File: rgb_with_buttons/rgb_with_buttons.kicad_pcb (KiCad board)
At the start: 2 copper layers, 17 parts, among them J4 Barrel_Jack_Switch, SW1 SW_MEC_5E, SW2 SW_MEC_5E, SW3 SW_MEC_5E, U1 ATmega328P-P

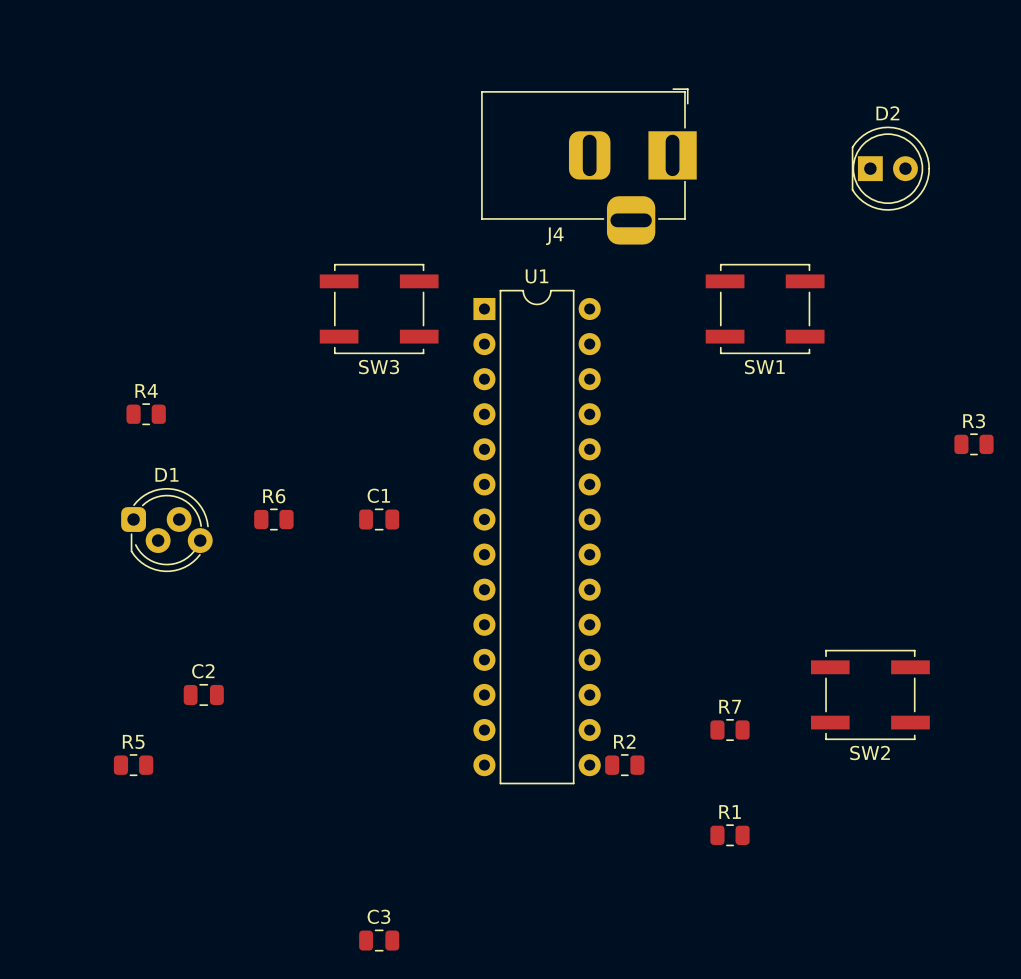
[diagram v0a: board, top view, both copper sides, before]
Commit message: all pcb is ready, not quite beautiful but functioning
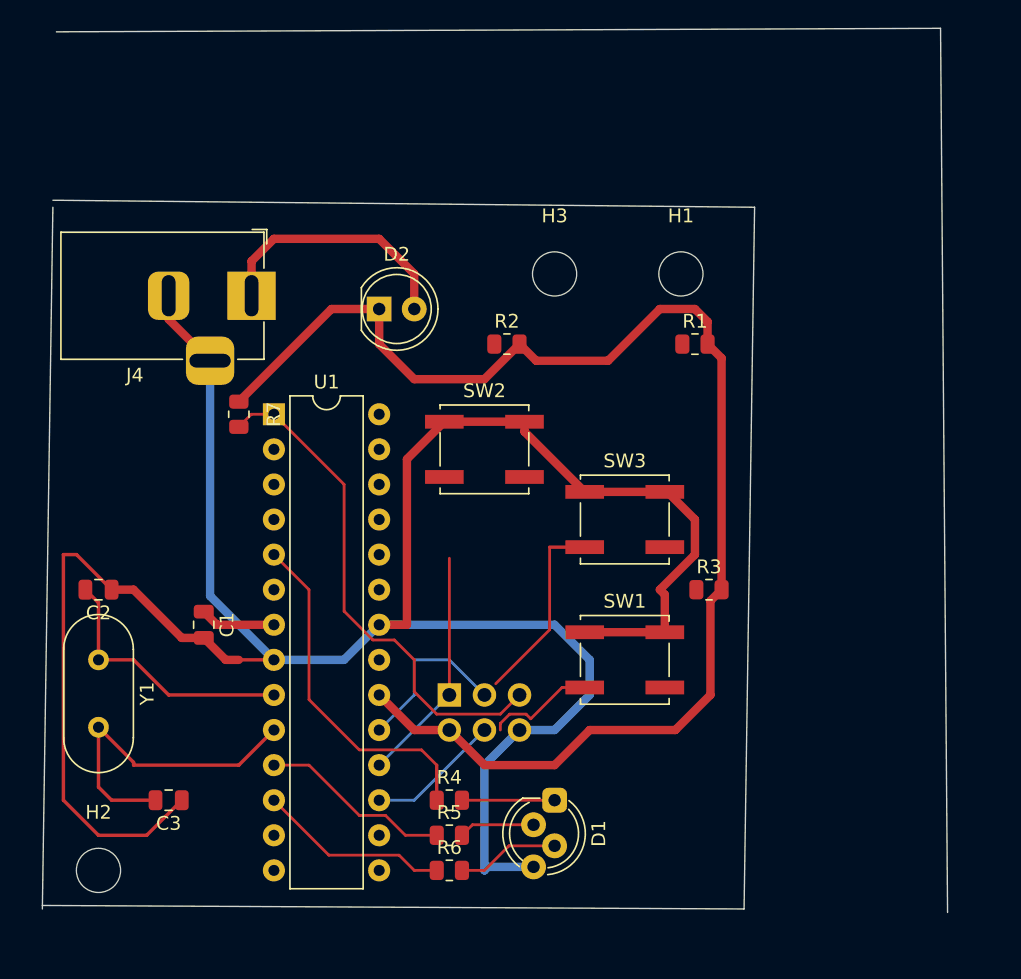
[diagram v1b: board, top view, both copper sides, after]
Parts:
- added H1: MountingHole, MountingHole:MountingHole_3.2mm_M3, F.Cu at (131.1, 81.3)
- added H2: MountingHole, MountingHole:MountingHole_3.2mm_M3, F.Cu at (88.9, 124.5)
- added H3: MountingHole, MountingHole:MountingHole_3.2mm_M3, F.Cu at (121.9, 81.3)
- added J1: ISP, Connector_PinHeader_2.54mm:PinHeader_2x03_P2.54mm_Vertical, B.Cu at (114.3, 111.8)
- added Y1: Crystal, Crystal:Crystal_HC49-4H_Vertical, F.Cu at (88.9, 109.2)
- moved R7 42.3 mm to (99.1, 91.4), turned to -90 degrees
- moved D2 37.0 mm to (109.2, 83.8)
- moved D1 36.6 mm to (121.9, 119.4), turned to -90 degrees
- moved R1 35.7 mm to (132.1, 86.4)
- moved R4 35.5 mm to (114.3, 119.4)
- moved SW2 33.1 mm to (116.8, 94.0), turned to 180 degrees
- moved J4 32.1 mm to (100.0, 82.9)
- moved R2 31.7 mm to (118.5, 86.4)
- moved R6 28.4 mm to (114.3, 124.5)
- moved SW1 27.4 mm to (127.0, 109.2), turned to 180 degrees
- moved SW3 23.4 mm to (127.0, 99.1), turned to 180 degrees
- moved R5 23.4 mm to (114.3, 121.9)
- moved R3 21.9 mm to (133.1, 104.1)
- moved C3 18.3 mm to (94.0, 119.4), turned to 180 degrees
- moved U1 17.0 mm to (101.6, 91.4)
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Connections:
- U1 pad 14: /8 -> unconnected-(U1-Pad14)
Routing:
- net GND: track 0.00 -> 179.4 mm
- net VCC: track 0.00 -> 105.2 mm
- net /RESET: track 0.00 -> 37.0 mm
- net /3: track 0.00 -> 25.3 mm
- net /XTAL2: track 0.00 -> 23.9 mm
- net /XTAL1: track 0.00 -> 19.2 mm
- net Net-(D2-Pad2): track 0.00 -> 18.5 mm
- net /MISO: track 0.00 -> 17.1 mm
- net unconnected-(SW3-Pad1): track 0.00 -> 14.0 mm
- net /5: track 0.00 -> 13.9 mm
- net /6: track 0.00 -> 13.9 mm
- net /SCK: track 0.00 -> 12.3 mm
- net /MOSI: track 0.00 -> 9.72 mm
- net unconnected-(SW1-Pad1): track 0.00 -> 7.94 mm
- net Net-(D1-Pad3): track 0.00 -> 7.44 mm
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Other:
- board outline added: 65.5 x 64 mm

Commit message: pcb is now complete(only warnings in DRC due to problem of the led design), had to change the symbol of the button a bit(nothing significant pin numbers only)
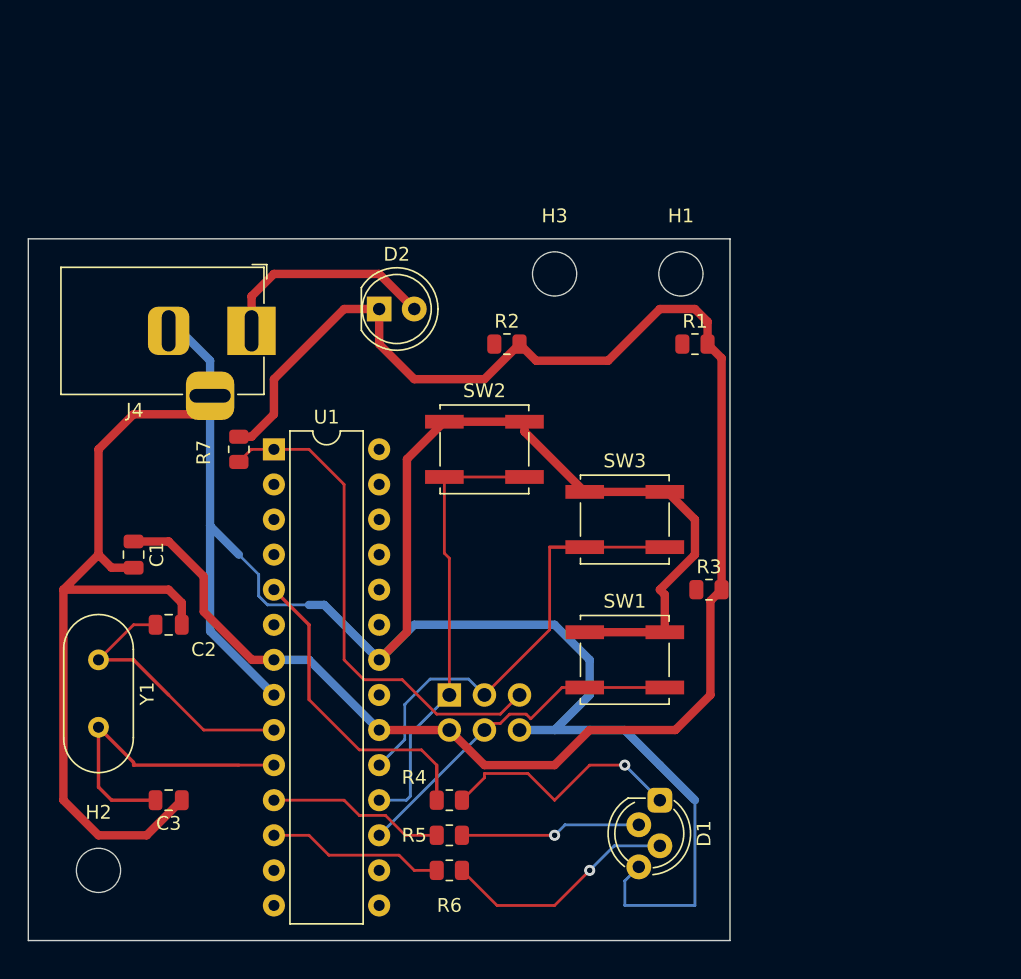
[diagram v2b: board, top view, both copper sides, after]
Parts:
- moved D1 7.62 mm to (129.5, 119.4)
- moved C1 7.18 mm to (91.4, 101.6)
- moved C2 5.68 mm to (94.0, 106.7)
- moved J4 2.54 mm to (100.0, 85.4)
- moved R7 2.54 mm to (99.1, 94.0)
- moved U1 2.54 mm to (101.6, 94.0)
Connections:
- SW1 pad 1: unconnected-(SW1-Pad1) -> /MOSI
- SW2 pad 1: unconnected-(SW2-Pad1) -> /MISO
- SW3 pad 1: unconnected-(SW3-Pad1) -> /SCK
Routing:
- net GND: track 179.4 -> 217.5 mm
- net VCC: track 105.2 -> 126.2 mm
- net /SCK: track 12.3 -> 33.2 mm
- net /MOSI: track 9.72 -> 25.4 mm
- net /MISO: track 17.1 -> 32.6 mm
- net unconnected-(SW3-Pad1): track 14.0 -> 0.00 mm
- net Net-(D1-Pad1): track 6.71 -> 18.2 mm, vias 0 -> 1
- net Net-(D1-Pad3): track 7.44 -> 17.2 mm, vias 0 -> 1
- net unconnected-(SW1-Pad1): track 7.94 -> 0.00 mm
- net Net-(D1-Pad2): track 5.50 -> 13.1 mm, vias 0 -> 1
- net /3: track 25.3 -> 22.8 mm
- net Net-(D2-Pad2): track 18.5 -> 16.0 mm
- net /XTAL2: track 23.9 -> 22.4 mm
- net /6: track 13.9 -> 12.8 mm
- net /5: track 13.9 -> 12.8 mm
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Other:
- board size 65.5 x 64 mm -> 50.8 x 50.8 mm
